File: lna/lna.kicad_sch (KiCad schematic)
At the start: 18 parts, among them J1 Conn_Coaxial, J2 V5-GND, J3 Conn_Coaxial, U1 PGA-103+

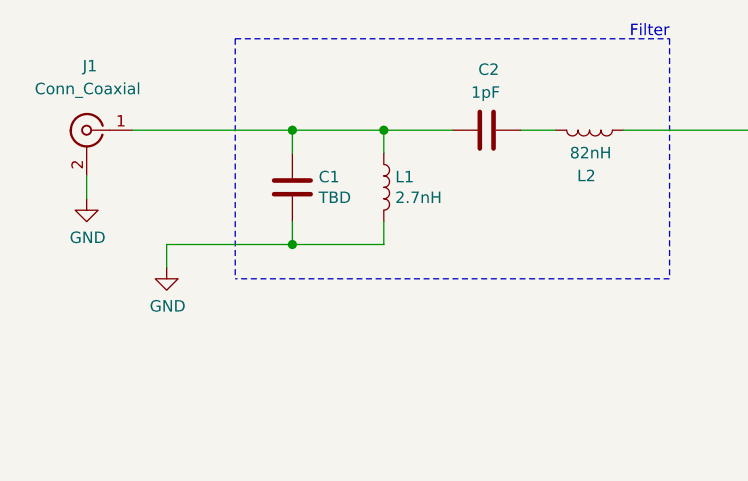
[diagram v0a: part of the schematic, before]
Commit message: Add proper component value
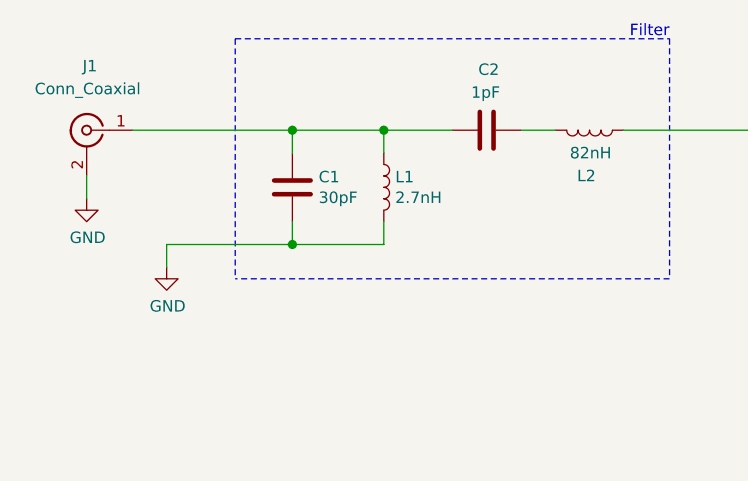
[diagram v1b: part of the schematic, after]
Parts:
- C1: value TBD -> 30pF
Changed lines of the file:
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@@
       (effects (font (size 1.27 1.27)) (justify left))
     )
-    (property "Value" "TBD" (id 1) (at 54.991 48.139 0)
+    (property "Value" "30pF" (id 1) (at 54.991 48.139 0)
       (effects (font (size 1.27 1.27)) (justify left))
     )
@@
     )
     (path "/e3613cca-fb62-4c1e-9e92-3c0f2f895470"
-      (reference "C1") (unit 1) (value "TBD") (footprint "Capacitor_SMD:C_0603_1608Metric")
+      (reference "C1") (unit 1) (value "30pF") (footprint "Capacitor_SMD:C_0603_1608Metric")
     )
     (path "/4de7368e-cf8f-457d-894b-7cde015e5ae4"
